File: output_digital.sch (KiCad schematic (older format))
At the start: 20 parts, among them J4 Screw_Terminal_1x02, J5 Screw_Terminal_1x02, J6 Screw_Terminal_1x02, Q1 MMBT3904, Q2 MMBT3904, U4 G2RL-1A-E, U6 G2RL-1A-E

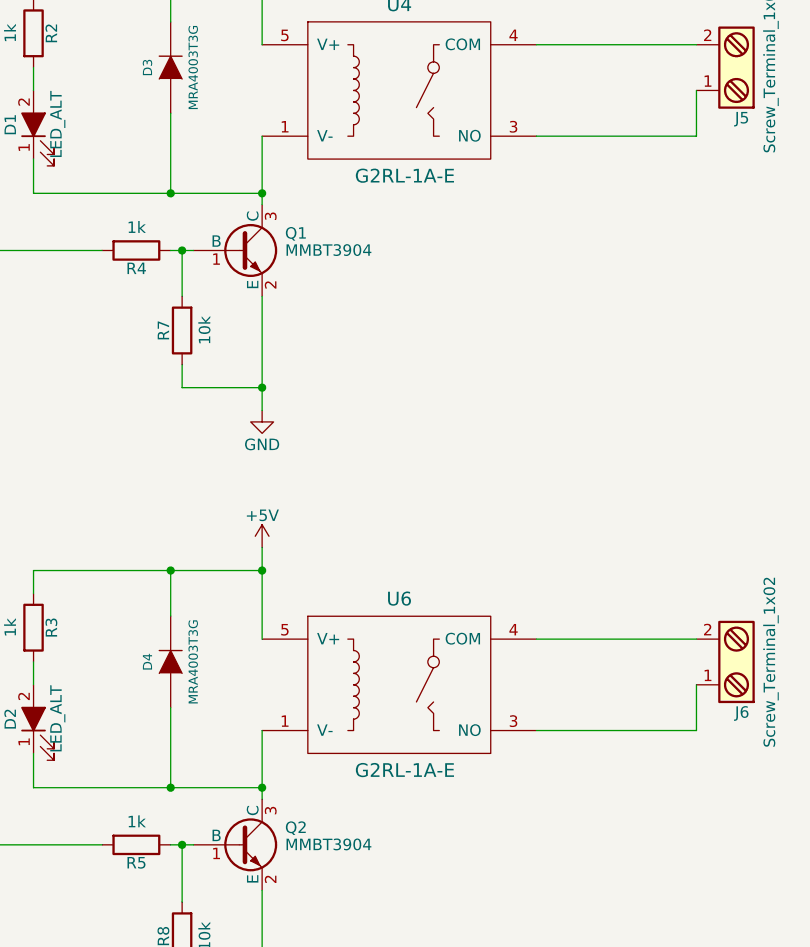
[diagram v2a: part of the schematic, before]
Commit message: Correciones y ubicacion en pcb
Se corrige problema con archivo inputs_temp.sch
Se corrige problema con footprints de Realys y transistores U4 y U6
Se hace primera ubicacion tentativa en PCB de componentes.
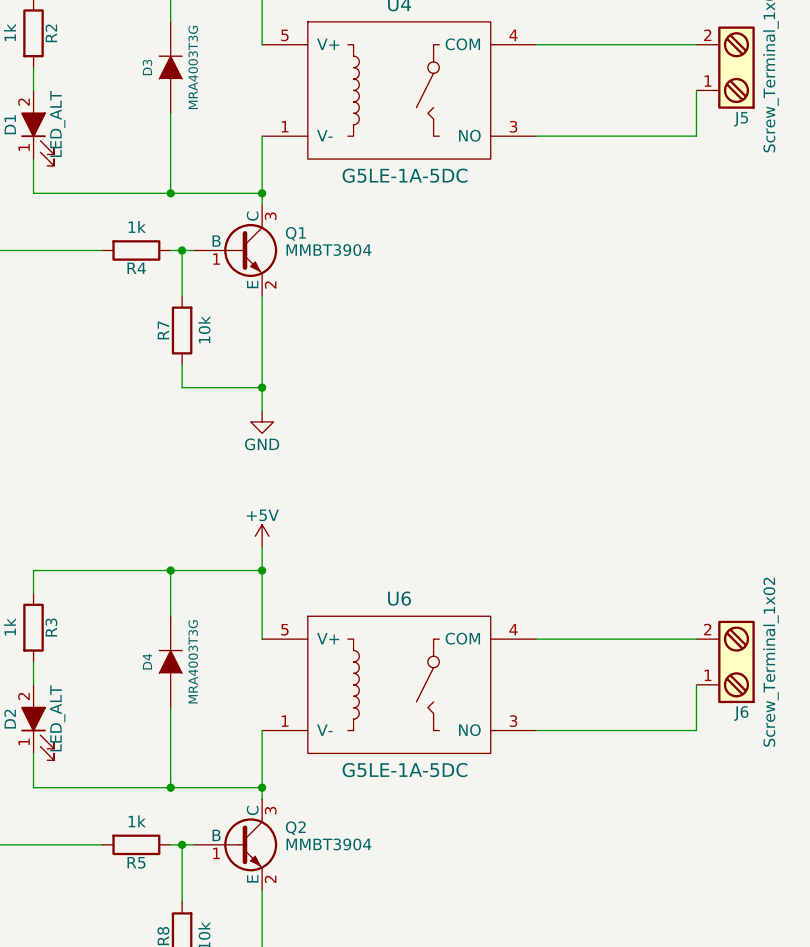
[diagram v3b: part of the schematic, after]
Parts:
- Q1, Q2: footprint footprints:SOT23GDS -> footprints:SOT23_NPN
- U4, U6: value G2RL-1A-E -> G5LE-1A-5DC; footprint footprints:Relay_SPST_Schrack-RP-II-1_RM3-5mm -> (none); Description General Purpose Relays 1 form A w/ TV3 5VDC Coil, 16A -> (none); Digikey# Value -> (none); Manf Omron Electronics -> (none); Manf# G2RL-1A-E-ASI DC5 -> (none); Mouser# 653-G2RL1AEASIDC5 -> (none)
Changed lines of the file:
@@
 $EndComp
 $Comp
-L +5V #PWR15
+L +5V #PWR015
 U 1 1 5949AA7B
 P 3900 2550
-F 0 "#PWR15" H 3900 2400 50  0001 C CNN
+F 0 "#PWR015" H 3900 2400 50  0001 C CNN
 F 1 "+5V" H 3900 2690 50  0000 C CNN
 F 2 "" H 3900 2550 50  0001 C CNN
@@
 $EndComp
 $Comp
-L GND #PWR16
+L GND #PWR016
 U 1 1 5949AA9F
 P 3900 4550
-F 0 "#PWR16" H 3900 4300 50  0001 C CNN
+F 0 "#PWR016" H 3900 4300 50  0001 C CNN
 F 1 "GND" H 3900 4400 50  0000 C CNN
 F 2 "" H 3900 4550 50  0001 C CNN
@@
 	5100 2950 5800 2950
 $Comp
-L +5V #PWR17
+L +5V #PWR017
 U 1 1 594AF973
 P 3900 5150
-F 0 "#PWR17" H 3900 5000 50  0001 C CNN
+F 0 "#PWR017" H 3900 5000 50  0001 C CNN
 F 1 "+5V" H 3900 5290 50  0000 C CNN
 F 2 "" H 3900 5150 50  0001 C CNN
@@
 $EndComp
 $Comp
-L GND #PWR18
+L GND #PWR018
 U 1 1 594AF979
 P 3900 7150
-F 0 "#PWR18" H 3900 6900 50  0001 C CNN
+F 0 "#PWR018" H 3900 6900 50  0001 C CNN
 F 1 "GND" H 3900 7000 50  0000 C CNN
 F 2 "" H 3900 7150 50  0001 C CNN
@@
 F 0 "Q1" H 4000 3925 50  0000 L CNN
 F 1 "MMBT3904" H 4000 3850 50  0000 L CNN
-F 2 "footprints:SOT23GDS" H 4000 3775 50  0001 L CIN
+F 2 "footprints:SOT23_NPN" H 4000 3775 50  0001 L CIN
 F 3 "2N3904-82270.pdf" H 3800 3850 50  0001 L CNN
 F 4 "ON Semiconductor" H 3800 3850 60  0001 C CNN "Manf"
@@
 	3900 1850 3900 1950
 $Comp
-L GND #PWR14
+L GND #PWR019
 U 1 1 594DE1D3
 P 3900 1950
-F 0 "#PWR14" H 3900 1700 50  0001 C CNN
+F 0 "#PWR019" H 3900 1700 50  0001 C CNN
 F 1 "GND" H 3900 1800 50  0000 C CNN
 F 2 "" H 3900 1950 50  0001 C CNN
@@
 $EndComp
 $Comp
-L GND #PWR19
+L GND #PWR020
 U 1 1 594DE220
 P 4800 1450
-F 0 "#PWR19" H 4800 1200 50  0001 C CNN
+F 0 "#PWR020" H 4800 1200 50  0001 C CNN
 F 1 "GND" H 4800 1300 50  0000 C CNN
 F 2 "" H 4800 1450 50  0001 C CNN
@@
 $EndComp
 $Comp
-L G5LE-1A-5DC U6
-U 1 1 594F1121
-P 4500 5750
-F 0 "U6" H 4500 6125 60  0000 C CNN
-F 1 "G2RL-1A-E" H 4525 5375 60  0000 C CNN
-F 2 "footprints:Relay_SPST_Schrack-RP-II-1_RM3-5mm" H 4500 5750 60  0001 C CNN
-F 3 "en-g2rl-472571.pdf" H 4500 5750 60  0001 C CNN
-F 4 "Omron Electronics" H 4500 5750 60  0001 C CNN "Manf"
-F 5 "G2RL-1A-E-ASI DC5" H 4500 5750 60  0001 C CNN "Manf#"
-F 6 "Value" H 4500 5750 60  0001 C CNN "Digikey#"
-F 7 "653-G2RL1AEASIDC5" H 4500 5750 60  0001 C CNN "Mouser#"
-F 8 "General Purpose Relays 1 form A w/ TV3 5VDC Coil, 16A" H 4500 5750 60  0001 C CNN "Description"
-	1    4500 5750
-	1    0    0    -1
-$EndComp
-$Comp
 L MMBT3904 Q2
 U 1 1 594F167D
@@
 F 0 "Q2" H 4000 6525 50  0000 L CNN
 F 1 "MMBT3904" H 4000 6450 50  0000 L CNN
-F 2 "footprints:SOT23GDS" H 4000 6375 50  0001 L CIN
+F 2 "footprints:SOT23_NPN" H 4000 6375 50  0001 L CIN
 F 3 "2N3904-82270.pdf" H 3800 6450 50  0001 L CNN
 F 4 "ON Semiconductor" H 3800 6450 60  0001 C CNN "Manf"
@@
 	3550 7050 3550 7000
 Connection ~ 3900 7050
+Wire Notes Line
+	7600 2600 6550 2600
 $Comp
 L G5LE-1A-5DC U4
-U 1 1 59510F67
+U 1 1 595B78E3
 P 4500 3150
 F 0 "U4" H 4500 3525 60  0000 C CNN
-F 1 "G2RL-1A-E" H 4525 2775 60  0000 C CNN
-F 2 "footprints:Relay_SPST_Schrack-RP-II-1_RM3-5mm" H 4500 3150 60  0001 C CNN
-F 3 "en-g2rl-472571.pdf" H 4500 3150 60  0001 C CNN
-F 4 "Omron Electronics" H 4500 3150 60  0001 C CNN "Manf"
-F 5 "G2RL-1A-E-ASI DC5" H 4500 3150 60  0001 C CNN "Manf#"
-F 6 "Value" H 4500 3150 60  0001 C CNN "Digikey#"
-F 7 "653-G2RL1AEASIDC5" H 4500 3150 60  0001 C CNN "Mouser#"
-F 8 "General Purpose Relays 1 form A w/ TV3 5VDC Coil, 16A" H 4500 3150 60  0001 C CNN "Description"
+F 1 "G5LE-1A-5DC" H 4525 2775 60  0000 C CNN
+F 2 "" H 4500 3150 60  0001 C CNN
+F 3 "" H 4500 3150 60  0001 C CNN
 	1    4500 3150
 	1    0    0    -1
 $EndComp
-Wire Notes Line
-	7600 2600 6550 2600
+$Comp
+L G5LE-1A-5DC U6
+U 1 1 595B7E68
+P 4500 5750
+F 0 "U6" H 4500 6125 60  0000 C CNN
+F 1 "G5LE-1A-5DC" H 4525 5375 60  0000 C CNN
+F 2 "" H 4500 5750 60  0001 C CNN
+F 3 "" H 4500 5750 60  0001 C CNN
+	1    4500 5750
+	1    0    0    -1
+$EndComp
 $EndSCHEMATC

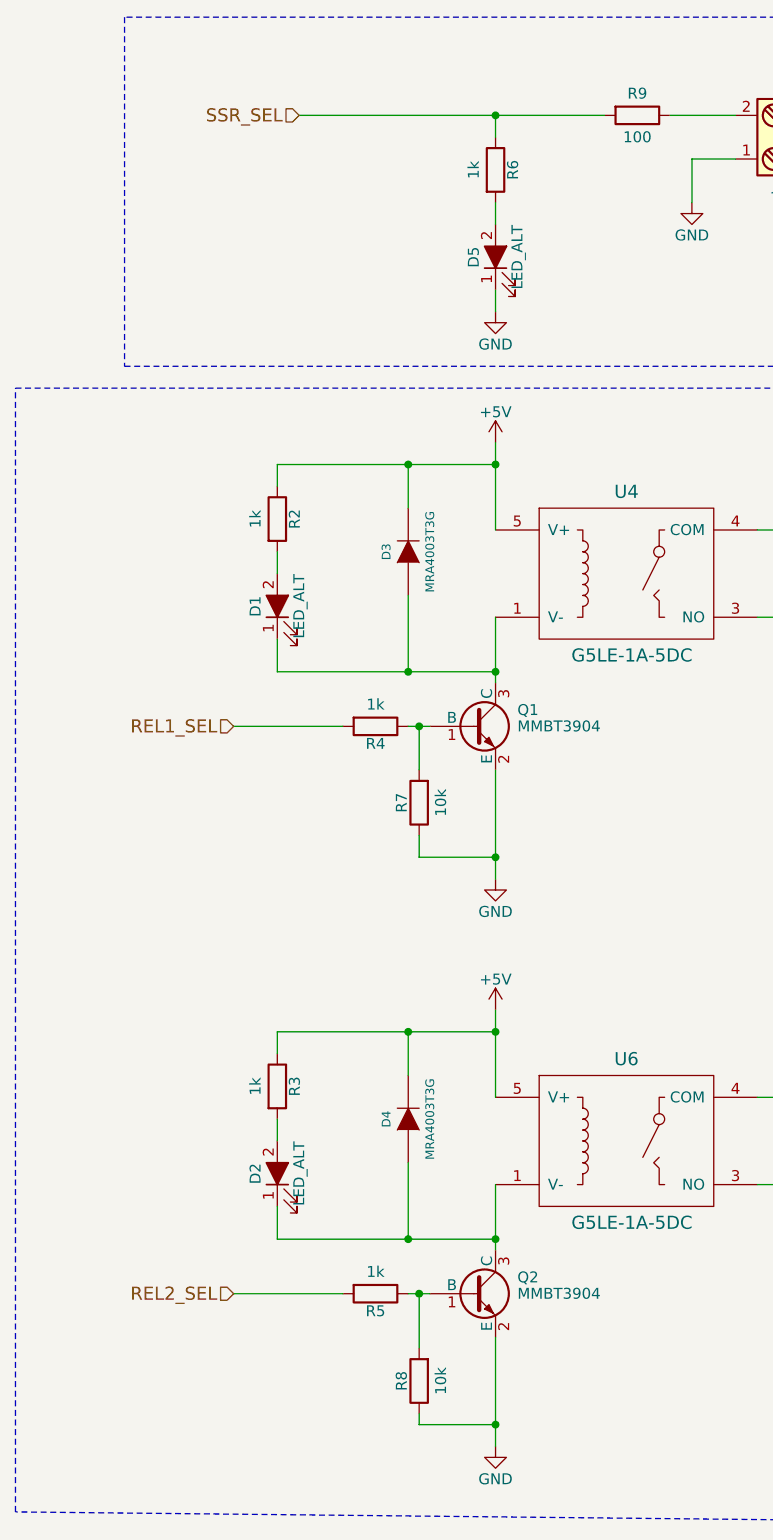
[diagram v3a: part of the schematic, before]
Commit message: Primer version del PCB
Se agregan modificaciones segun primer correccion. Se carga primer version  del PCB.
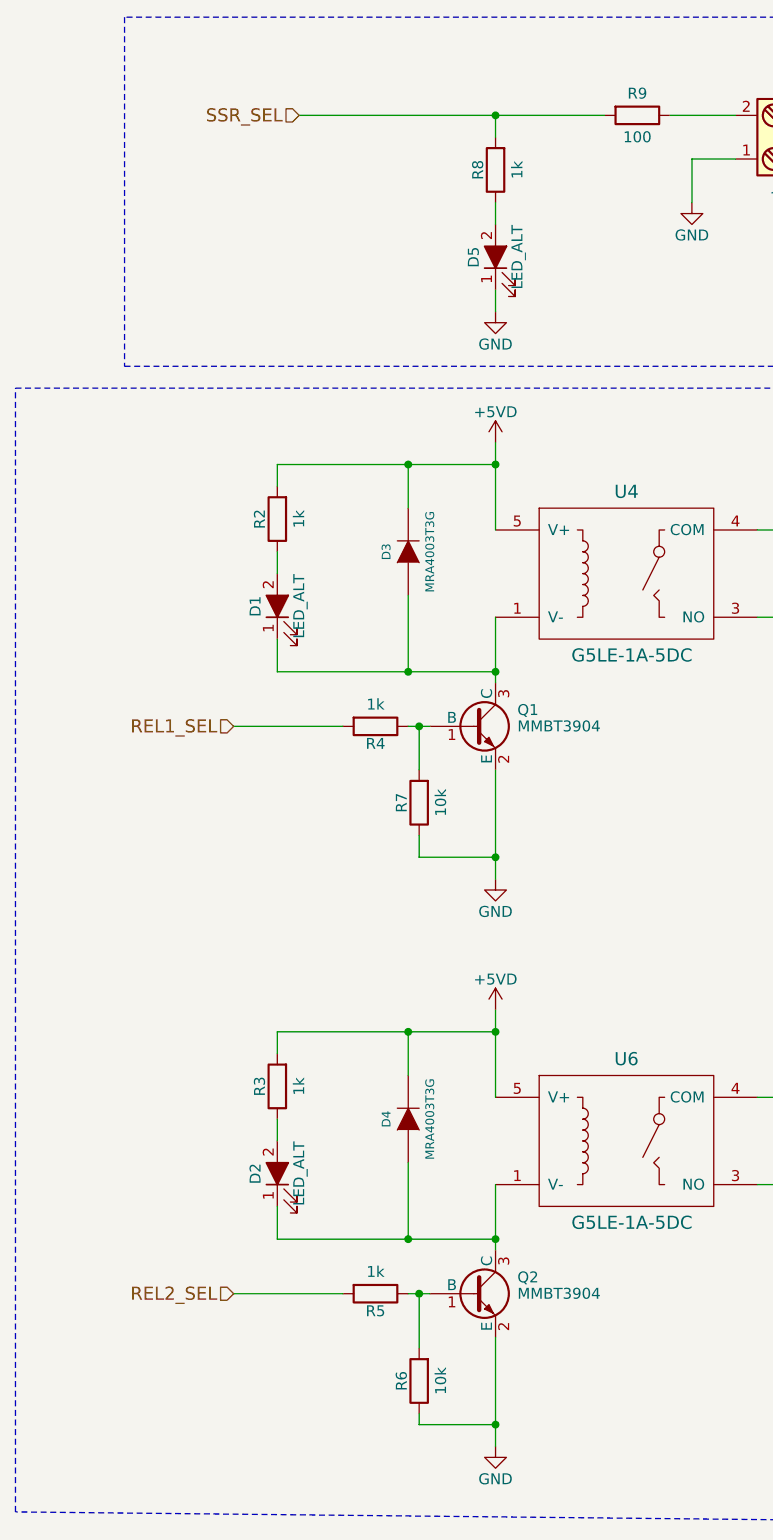
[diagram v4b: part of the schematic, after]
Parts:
- R2, R3, R4, R5: footprint footprints:R_1206_HandSoldering -> footprints:R_0805_HandSoldering; Description 1k Ohm ±1% 0.25W, 1/4W Chip Resistor 1206 (3216 Metric) Moi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 -> Thick Film Resistors - SMD 1K OHM 1%; Digikey# 311-1.00KFRTR-ND -> 311-1.00KCRCT-ND; Manf# RC1206FR-071KL -> RC0805FR-071KL; Mouser# Value -> 603-RC0805FR-071KL
- R6: value 1k -> 10k; footprint footprints:R_1206_HandSoldering -> footprints:R_0805_HandSoldering; Description 1k Ohm ±1% 0.25W, 1/4W Chip Resistor 1206 (3216 Metric) Moi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 -> Thick Film Resistors - SMD 10K OHM 1%; Digikey# 311-1.00KFRTR-ND -> 311-10.0KCRCT-ND; Manf# RC1206FR-071KL -> RC0805FR-0710KL; Mouser# Value -> 603-RC0805FR-0710KL
- R7: footprint footprints:R_1206_HandSoldering -> footprints:R_0805_HandSoldering; Description 10k Ohm ±5% 0.25W, 1/4W Chip, Moisture Resistant Thick Film -> Thick Film Resistors - SMD 10K OHM 1%; Digikey# 311-10KERTR-ND -> 311-10.0KCRCT-ND; Manf# RC1206JR-0710KL -> RC0805FR-0710KL; Mouser# Value -> 603-RC0805FR-0710KL
- R8: value 10k -> 1k; footprint footprints:R_1206_HandSoldering -> footprints:R_0805_HandSoldering; Description 10k Ohm ±5% 0.25W, 1/4W Chip, Moisture Resistant Thick Film -> Thick Film Resistors - SMD 1K OHM 1%; Digikey# 311-10KERTR-ND -> 311-1.00KCRCT-ND; Manf# RC1206JR-0710KL -> RC0805FR-071KL; Mouser# Value -> 603-RC0805FR-071KL
- R9: footprint footprints:R_1206_HandSoldering -> footprints:R_0805_HandSoldering; Description 100 Ohm ±1% 0.25W, 1/4W Chip Resistor 1206 Moisture Resista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 -> 1Thick Film Resistors - SMD 100 OHM 1%; Digikey# 311-100FRTR-ND -> 311-100CRCT-ND; Manf Vishay -> Yageo; Manf# RC1206FR-07100RL -> RC0805FR-07100RL; Mouser# Value -> 603-RC0805FR-07100RL
- U4, U6: footprint (none) -> footprints:Relay_G5LE-1A-5DC-5mm
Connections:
- net GND: now also R6.1; no longer R8.1
- net SSR_SEL: now also R8.2; no longer R6.1
- net at D1.2 (A): now also R2.1; no longer R2.2
- net at D5.2 (A): now also R8.1; no longer R6.2
- net at Q2.1 (B), R5.1: now also R6.2; no longer R8.2
- net at D2.2 (A): now also R3.1; no longer R3.2
- net +5V renamed +5VD
- net +5VD: now also R2.2, R3.2; no longer R2.1, R3.1

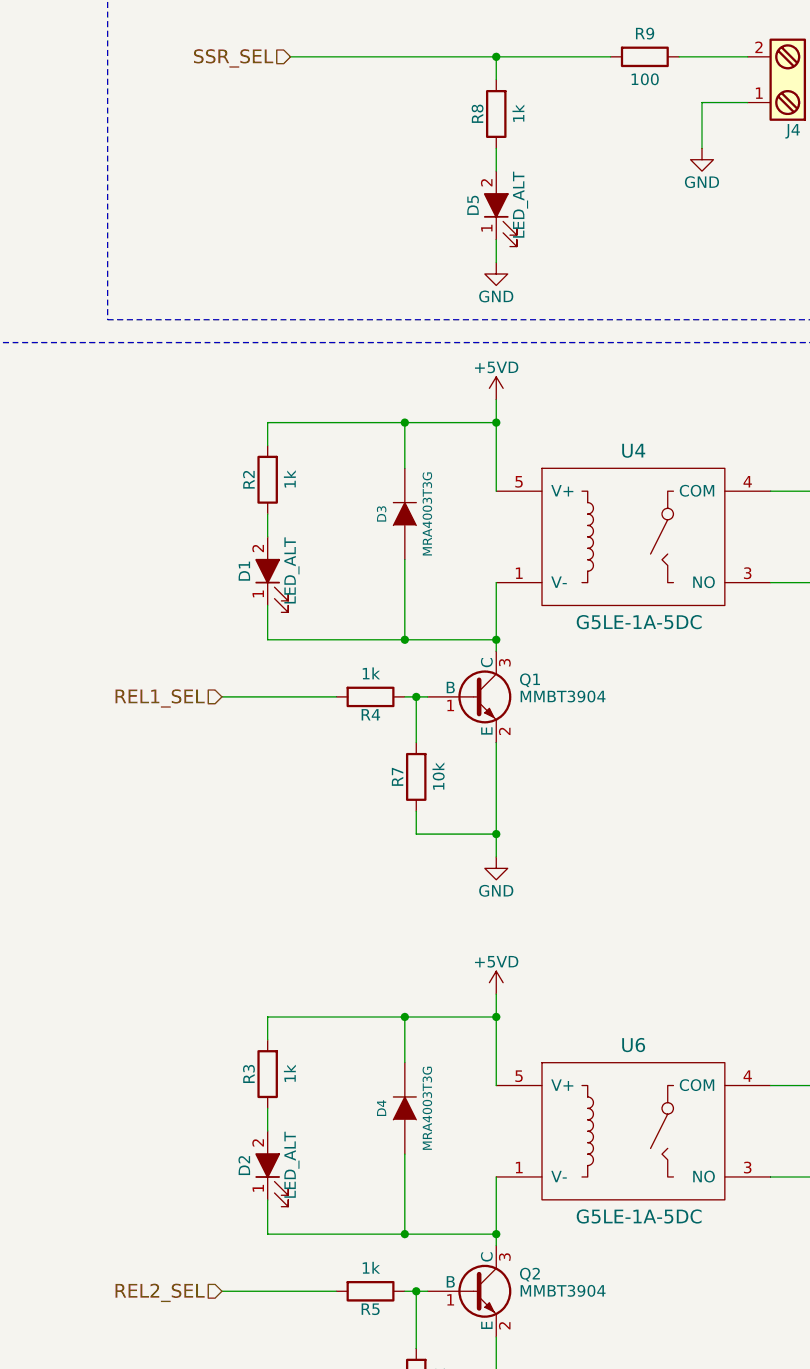
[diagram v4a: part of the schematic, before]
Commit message: Correccion Final
Se trabajo sobre correcciones de 2da revision. Se agregaron archivos gerbers, BOM, y objetos 3D
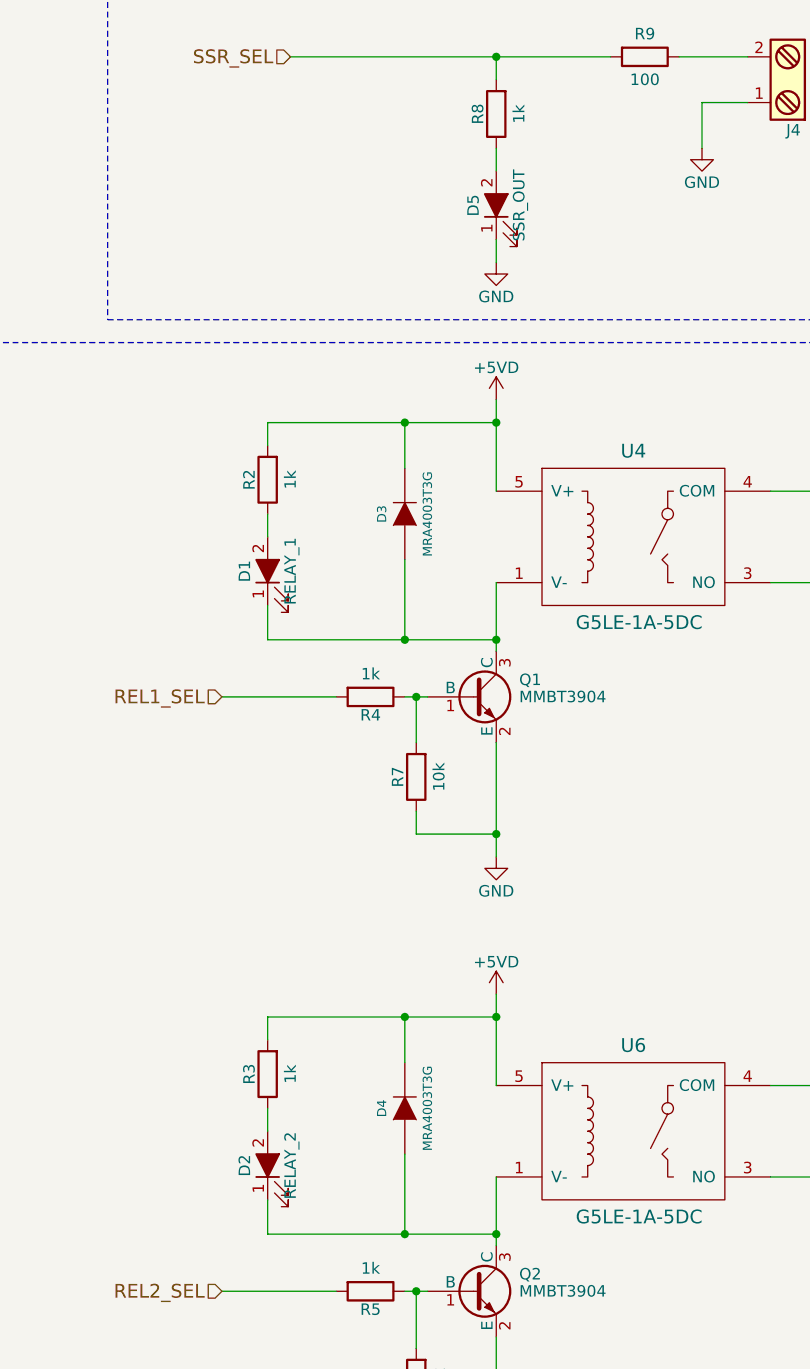
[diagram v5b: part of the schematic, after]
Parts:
- D1: value LED_ALT -> RELAY_1
- D2: value LED_ALT -> RELAY_2
- D5: value LED_ALT -> SSR_OUT
- U4, U6: Description (none) -> General Purpose Relays SPST-NO 5VDC 79.4mA; Digikey# (none) -> Z3115-ND; Manf (none) -> Omron Electronics; Manf# (none) -> G5LE-1A DC5; Mouser# (none) -> 653-G5LE-1ADC5
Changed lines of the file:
@@
 EESchema Schematic File Version 2
 LIBS:TempRelay
-LIBS:power
-LIBS:tempRelayPoncho-cache
 EELAYER 25 0
 EELAYER END
@@
 P 3900 1700
 F 0 "D5" H 3900 1800 50  0000 C CNN
-F 1 "LED_ALT" H 3900 1600 50  0000 C CNN
+F 1 "SSR_OUT" H 3900 1600 50  0000 C CNN
 F 2 "footprints:LED-0805" H 3900 1700 50  0001 C CNN
 F 3 "qtlp630c-2.pdf" H 3900 1700 50  0001 C CNN
@@
 P 2900 3300
 F 0 "D1" H 2900 3400 50  0000 C CNN
-F 1 "LED_ALT" H 2900 3200 50  0000 C CNN
+F 1 "RELAY_1" H 2900 3200 50  0000 C CNN
 F 2 "footprints:LED-0805" H 2900 3300 50  0001 C CNN
 F 3 "qtlp630c-2.pdf" H 2900 3300 50  0001 C CNN
@@
 P 2900 5900
 F 0 "D2" H 2900 6000 50  0000 C CNN
-F 1 "LED_ALT" H 2900 5800 50  0000 C CNN
+F 1 "RELAY_2" H 2900 5800 50  0000 C CNN
 F 2 "footprints:LED-0805" H 2900 5900 50  0001 C CNN
 F 3 "qtlp630c-2.pdf" H 2900 5900 50  0001 C CNN
@@
 F 1 "G5LE-1A-5DC" H 4525 2775 60  0000 C CNN
 F 2 "footprints:Relay_G5LE-1A-5DC-5mm" H 4500 3150 60  0001 C CNN
-F 3 "" H 4500 3150 60  0001 C CNN
+F 3 "G5LE_0813-267607.pdf" H 4500 3150 60  0001 C CNN
+F 4 "Omron Electronics" H 4500 3150 60  0001 C CNN "Manf"
+F 5 "G5LE-1A DC5" H 4500 3150 60  0001 C CNN "Manf#"
+F 6 "Z3115-ND" H 4500 3150 60  0001 C CNN "Digikey#"
+F 7 "653-G5LE-1ADC5" H 4500 3150 60  0001 C CNN "Mouser#"
+F 8 "General Purpose Relays SPST-NO 5VDC 79.4mA" H 4500 3150 60  0001 C CNN "Description"
 	1    4500 3150
-	1    0    0    -1
-$EndComp
-$Comp
-L G5LE-1A-5DC U6
-U 1 1 595B7E68
-P 4500 5750
-F 0 "U6" H 4500 6125 60  0000 C CNN
-F 1 "G5LE-1A-5DC" H 4525 5375 60  0000 C CNN
-F 2 "footprints:Relay_G5LE-1A-5DC-5mm" H 4500 5750 60  0001 C CNN
-F 3 "" H 4500 5750 60  0001 C CNN
-	1    4500 5750
 	1    0    0    -1
 $EndComp
@@
 	1    0    0    -1
 $EndComp
+$Comp
+L G5LE-1A-5DC U6
+U 1 1 59879F2F
+P 4500 5750
+F 0 "U6" H 4500 6125 60  0000 C CNN
+F 1 "G5LE-1A-5DC" H 4525 5375 60  0000 C CNN
+F 2 "footprints:Relay_G5LE-1A-5DC-5mm" H 4500 5750 60  0001 C CNN
+F 3 "G5LE_0813-267607.pdf" H 4500 5750 60  0001 C CNN
+F 4 "Omron Electronics" H 4500 5750 60  0001 C CNN "Manf"
+F 5 "G5LE-1A DC5" H 4500 5750 60  0001 C CNN "Manf#"
+F 6 "Z3115-ND" H 4500 5750 60  0001 C CNN "Digikey#"
+F 7 "653-G5LE-1ADC5" H 4500 5750 60  0001 C CNN "Mouser#"
+F 8 "General Purpose Relays SPST-NO 5VDC 79.4mA" H 4500 5750 60  0001 C CNN "Description"
+	1    4500 5750
+	1    0    0    -1
+$EndComp
